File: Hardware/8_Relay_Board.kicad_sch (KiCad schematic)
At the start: 74 parts, among them J1 Conn_01x09, J10 Screw_Terminal_3.5mm_2, J2 Conn_01x09, J3 Screw_Terminal_3.5mm_4, J4 Screw_Terminal_3.5mm_4, J5 Screw_Terminal_3.5mm_4, J6 Screw_Terminal_3.5mm_4, J7 Screw_Terminal_3.5mm_4, J8 Screw_Terminal_3.5mm_4, J9 Barrel_Jack, U1 TLP627-4, U2 TLP627-4

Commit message: Close to finishing layout
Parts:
- removed J9: Barrel_Jack, SparkFun-Connector:POWER_JACK_PTH, symbol SparkFun-Connector:Barrel_Jack
- removed U1, U2: TLP627-4, SparkFun-Semiconductor-Standard:PDIP16, symbol SparkFun-IC-Special-Function:TLP627-4
- added J11: USB_C_Receptacle, SparkFun-Connector:USB-C-16P, symbol SparkFun-Connector:USB_C_Receptacle
- added R18, R19: 5.1k, SparkFun-Resistor:R_0603_1608Metric, symbol SparkFun-Resistor:5.1k_0603
- added U1, U2, U3, U4, U5, U6, U8, U9: TLP627, SparkFun-Semiconductor-Standard:DIP4, symbol SparkFun-IC-Special-Function:TLP627
- U7: footprint SparkFun-Aesthetic:Ordering_Instructions -> SparkFun-Aesthetic:ORDERING_INSTRUCTIONS
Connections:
- net +5V: now also J11.VBUS
- net COM1: now also J3.1 (Pin_1); no longer J3.2 (Pin_2)
- net COM2: now also J3.4 (Pin_4); no longer J4.1 (Pin_1)
- net COM3: now also J4.3 (Pin_3); no longer J4.4 (Pin_4)
- net COM4: now also J5.2 (Pin_2); no longer J5.3 (Pin_3)
- net COM5: now also J6.1 (Pin_1); no longer J6.2 (Pin_2)
- net COM6: now also J6.4 (Pin_4); no longer J7.1 (Pin_1)
- net COM7: now also J7.3 (Pin_3); no longer J7.4 (Pin_4)
- net COM8: now also J8.2 (Pin_2); no longer J8.3 (Pin_3)
- net GND: now also J11.GND, R18.2, R19.2, U1.3, U2.3, U3.3, U4.3, U5.3, U6.3, U8.3, U9.3
- net IN1: now also U3.1
- net IN2: now also U1.1
- net IN3: now also U2.1
- net IN4: now also U4.1
- net IN5: now also U5.1
- net IN6: now also U6.1
- net IN7: now also U8.1
- net IN8: now also U9.1
- net NC1: now also J3.2 (Pin_2); no longer J3.3 (Pin_3)
- net NC2: now also J4.1 (Pin_1); no longer J4.2 (Pin_2)
- net NC3: now also J4.4 (Pin_4); no longer J5.1 (Pin_1)
- net NC4: now also J5.3 (Pin_3); no longer J5.4 (Pin_4)
- net NC5: now also J6.2 (Pin_2); no longer J6.3 (Pin_3)
- net NC6: now also J7.1 (Pin_1); no longer J7.2 (Pin_2)
- net NC7: now also J7.4 (Pin_4); no longer J8.1 (Pin_1)
- net NC8: now also J8.3 (Pin_3); no longer J8.4 (Pin_4)
- net NO1: now also J3.3 (Pin_3); no longer J3.1 (Pin_1)
- net NO2: now also J4.2 (Pin_2); no longer J3.4 (Pin_4)
- net NO3: now also J5.1 (Pin_1); no longer J4.3 (Pin_3)
- net NO4: now also J5.4 (Pin_4); no longer J5.2 (Pin_2)
- net NO5: now also J6.3 (Pin_3); no longer J6.1 (Pin_1)
- net NO6: now also J7.2 (Pin_2); no longer J6.4 (Pin_4)
- net NO7: now also J8.1 (Pin_1); no longer J7.3 (Pin_3)
- net NO8: now also J8.4 (Pin_4); no longer J8.2 (Pin_2)
- net RELAY1: now also U4.4
- net RELAY2: now also U2.4
- net RELAY3: now also U1.4
- net RELAY4: now also U3.4
- net RELAY5: now also U9.4
- net RELAY6: now also U8.4
- net RELAY7: now also U6.4
- net RELAY8: now also U5.4
- net at R14.2: now also U6.2
- net at R10.2: now also U1.2
- net at R11.2: now also U2.2
- net at R13.2: now also U5.2
- net at R9.2: now also U3.2
- net at R16.2: now also U9.2
- net at R15.2: now also U8.2
- net at R12.2: now also U4.2
- new net: J11.A5 (CC1), R19.1
- new net: J11.B5 (CC2), R18.1
- new net: J11.A6 (D+), J11.B6 (D+)
- new net: J11.A7 (D-), J11.B7 (D-)
- new net: J11.A8 (NC), J11.B8 (NC)
- new net: J11.NC1 (NC), J11.NC2 (NC), J11.NC3 (NC)
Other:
- note added: "5VDC Input Header"
- note added: "USB Power Connector"
- note removed: "Power Connectors"
- moved on the sheet: D17, J10, JP9, R17

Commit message: Ready for final review
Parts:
- U1, U2, U3, U4, U5, U6, U8, U9: footprint SparkFun-Semiconductor-Standard:DIP4 -> SparkFun-Semiconductor-Standard:SMDIP4; symbol SparkFun-IC-Special-Function:TLP627 -> SparkFun-IC-Special-Function:TLP627(SMT)
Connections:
- net COM1: now also J3.2 (Pin_2); no longer J3.1 (Pin_1)
- net COM2: now also J4.1 (Pin_1); no longer J3.4 (Pin_4)
- net COM3: now also J4.4 (Pin_4); no longer J4.3 (Pin_3)
- net COM4: now also J5.3 (Pin_3); no longer J5.2 (Pin_2)
- net COM5: now also J6.2 (Pin_2); no longer J6.1 (Pin_1)
- net COM6: now also J7.1 (Pin_1); no longer J6.4 (Pin_4)
- net COM7: now also J7.4 (Pin_4); no longer J7.3 (Pin_3)
- net COM8: now also J8.3 (Pin_3); no longer J8.2 (Pin_2)
- net NC1: now also J3.1 (Pin_1); no longer J3.2 (Pin_2)
- net NC2: now also J3.4 (Pin_4); no longer J4.1 (Pin_1)
- net NC3: now also J4.3 (Pin_3); no longer J4.4 (Pin_4)
- net NC4: now also J5.2 (Pin_2); no longer J5.3 (Pin_3)
- net NC5: now also J6.1 (Pin_1); no longer J6.2 (Pin_2)
- net NC6: now also J6.4 (Pin_4); no longer J7.1 (Pin_1)
- net NC7: now also J7.3 (Pin_3); no longer J7.4 (Pin_4)
- net NC8: now also J8.2 (Pin_2); no longer J8.3 (Pin_3)

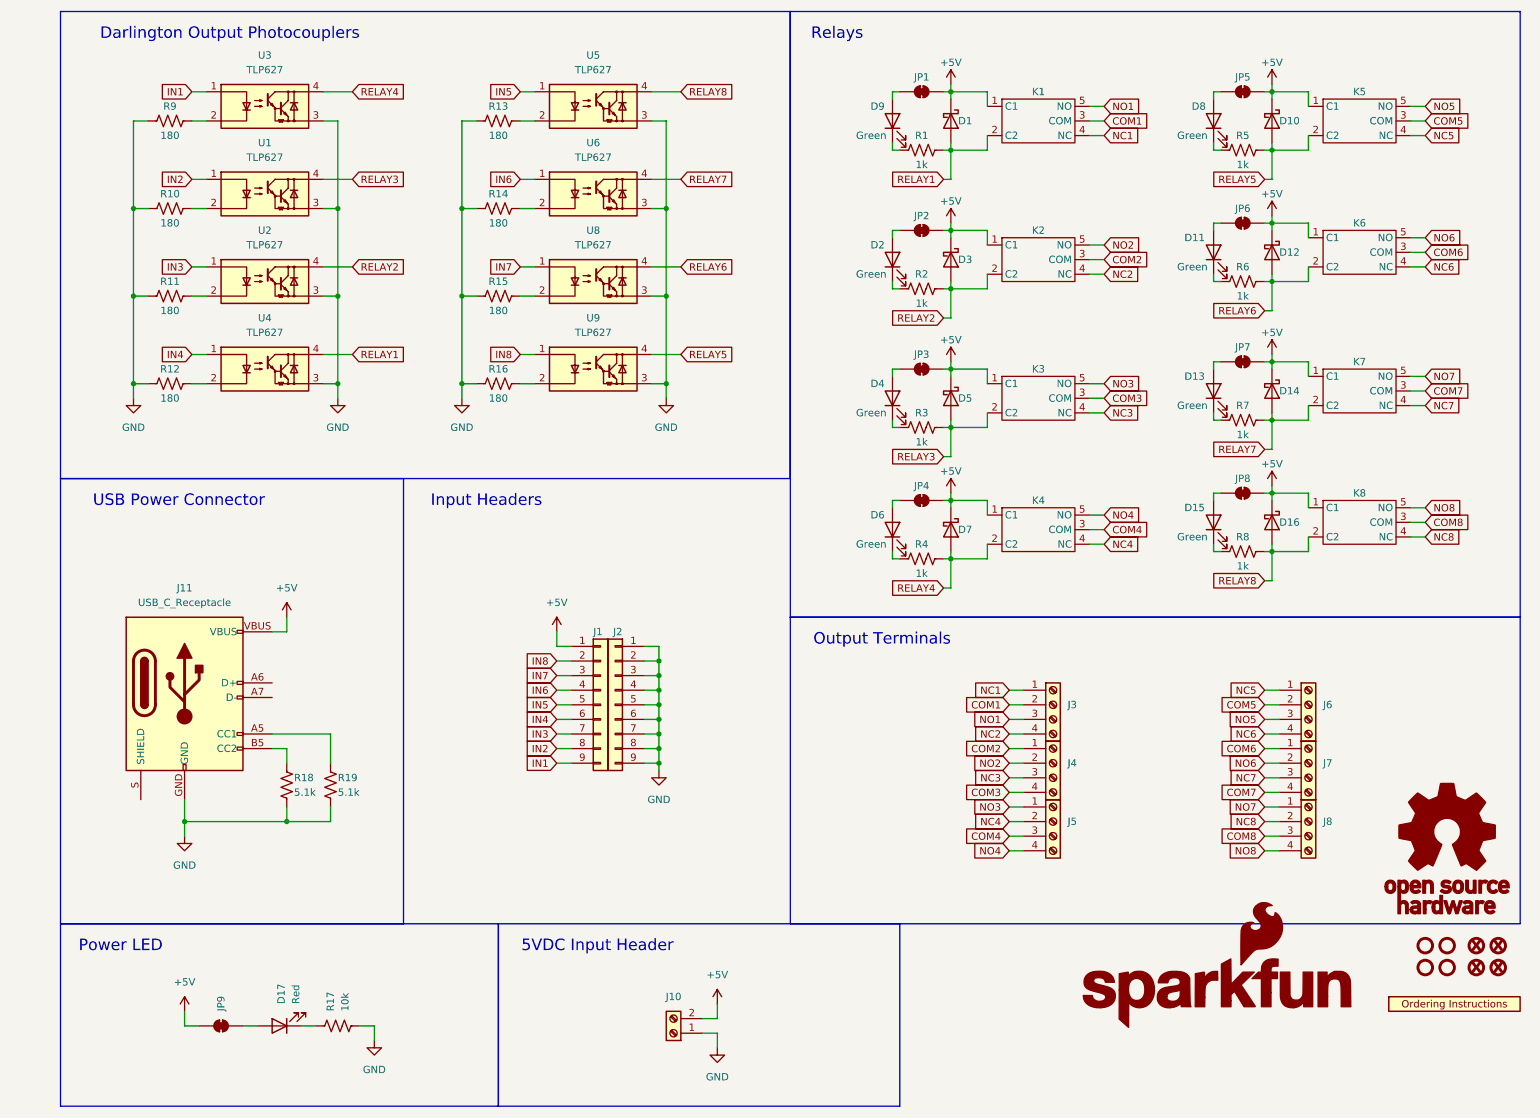
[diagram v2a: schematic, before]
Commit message: Second pre-release revision
- Add isolation under relays
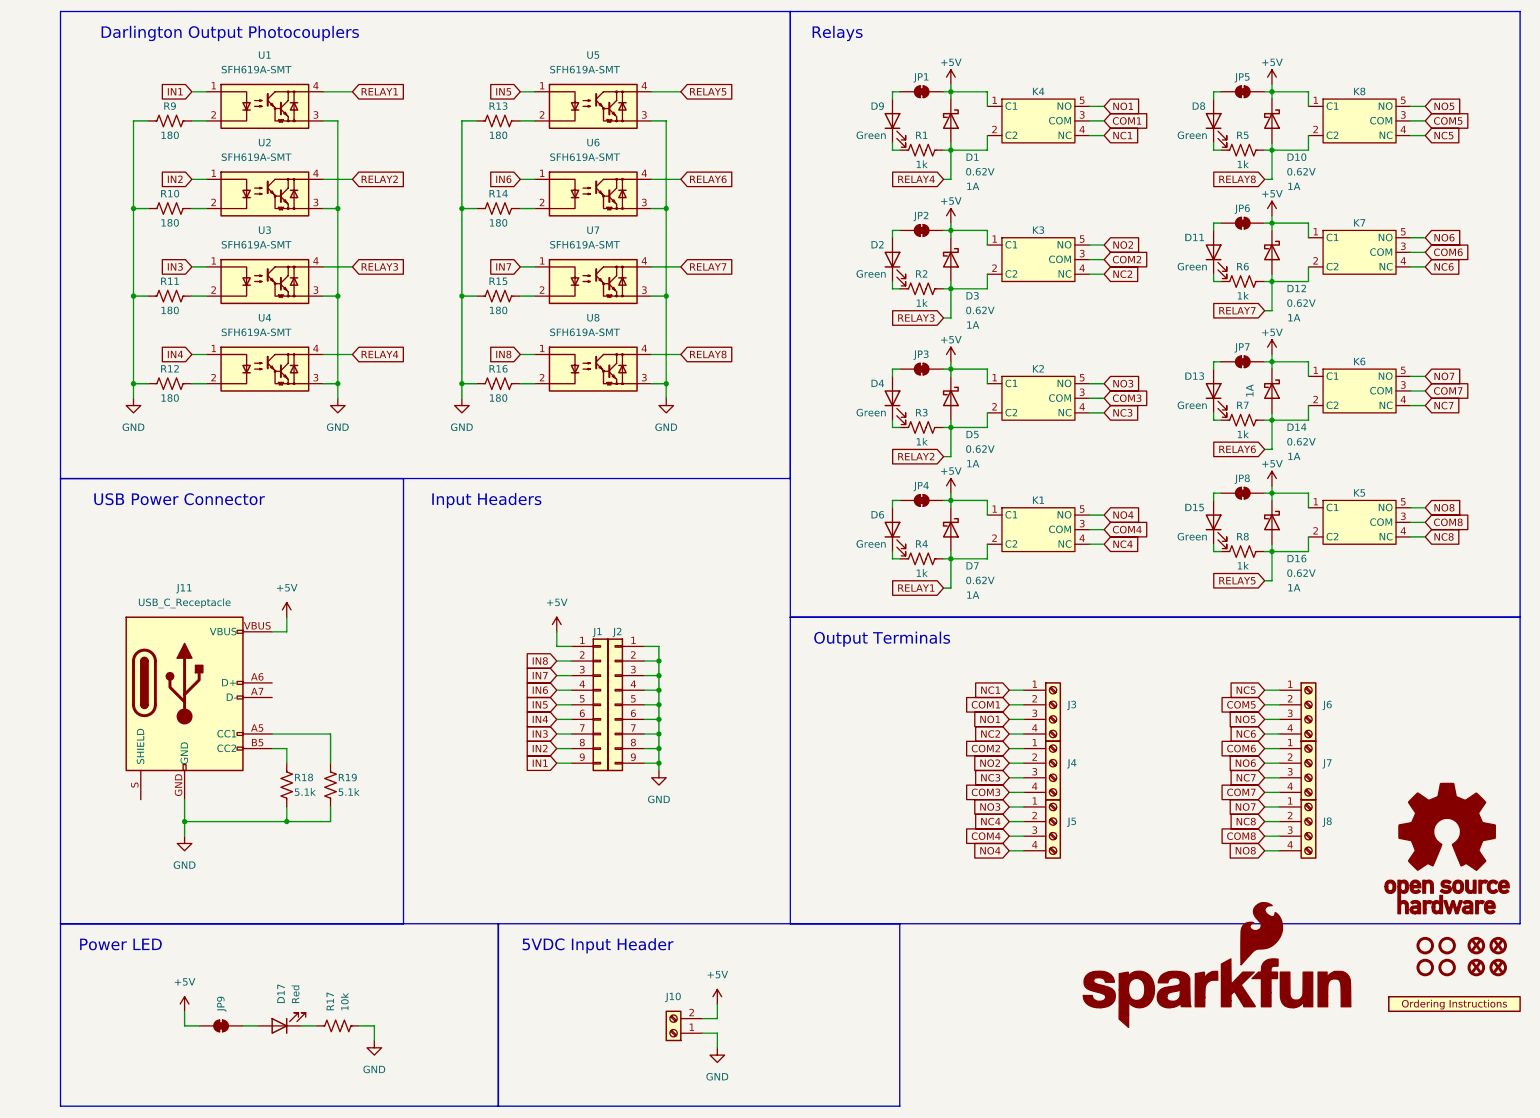
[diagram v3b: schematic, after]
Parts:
- D1, D10, D12, D16, D3, D5, D7: Current (none) -> 1A; VForward (none) -> 0.62V; VReverse (none) -> 23V
- D14: Current (none) -> 1A; Forward Current (none) -> 1A; Reverse Voltage (none) -> 23V; VForward (none) -> 0.62V; VReverse (none) -> 23V
- JP1, JP2, JP3, JP4, JP5, JP6, JP7, JP8, JP9: footprint SparkFun-Jumper:SMT-JUMPER_2_NC_TRACE_NO-SILK -> SparkFun-Jumper:SMT-JUMPER_2_NC_TRACE_SILK; symbol SparkFun-Jumper:SolderJumper_2_Bridged_No_Silk -> SparkFun-Jumper:SolderJumper_2_Bridged
- U1: renamed from U3; value TLP627 -> SFH619A-SMT; footprint SparkFun-Semiconductor-Standard:SMDIP4 -> SparkFun-Semiconductor-Standard:SMDIP4-WIDE; symbol SparkFun-IC-Special-Function:TLP627(SMT) -> SparkFun-IC-Special-Function:SFH619A-SMT
- U2: renamed from U1; value TLP627 -> SFH619A-SMT; footprint SparkFun-Semiconductor-Standard:SMDIP4 -> SparkFun-Semiconductor-Standard:SMDIP4-WIDE; symbol SparkFun-IC-Special-Function:TLP627(SMT) -> SparkFun-IC-Special-Function:SFH619A-SMT
- U3: renamed from U2; value TLP627 -> SFH619A-SMT; footprint SparkFun-Semiconductor-Standard:SMDIP4 -> SparkFun-Semiconductor-Standard:SMDIP4-WIDE; symbol SparkFun-IC-Special-Function:TLP627(SMT) -> SparkFun-IC-Special-Function:SFH619A-SMT
- U4, U5, U6: value TLP627 -> SFH619A-SMT; footprint SparkFun-Semiconductor-Standard:SMDIP4 -> SparkFun-Semiconductor-Standard:SMDIP4-WIDE; symbol SparkFun-IC-Special-Function:TLP627(SMT) -> SparkFun-IC-Special-Function:SFH619A-SMT
- U7: renamed from U8; value TLP627 -> SFH619A-SMT; footprint SparkFun-Semiconductor-Standard:SMDIP4 -> SparkFun-Semiconductor-Standard:SMDIP4-WIDE; symbol SparkFun-IC-Special-Function:TLP627(SMT) -> SparkFun-IC-Special-Function:SFH619A-SMT
- U8: renamed from U9; value TLP627 -> SFH619A-SMT; footprint SparkFun-Semiconductor-Standard:SMDIP4 -> SparkFun-Semiconductor-Standard:SMDIP4-WIDE; symbol SparkFun-IC-Special-Function:TLP627(SMT) -> SparkFun-IC-Special-Function:SFH619A-SMT
- renumbered K4 to K1, K3 to K2, K2 to K3, K1 to K4, K8 to K5, K7 to K6, K6 to K7, K5 to K8, U7 to U9
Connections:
- net RELAY1: now also D7.A, K1.2 (C2), R4.2, U1.4; no longer D1.A, K4.2 (C2), R1.2, U4.4
- net RELAY2: now also D5.A, K2.2 (C2), R3.2, U2.4; no longer D3.A, K3.2 (C2), R2.2, U3.4
- net RELAY3: now also D3.A, K3.2 (C2), R2.2, U3.4; no longer D5.A, K2.2 (C2), R3.2, U2.4
- net RELAY4: now also D1.A, K4.2 (C2), R1.2, U4.4; no longer D7.A, K1.2 (C2), R4.2, U1.4
- net RELAY5: now also D16.A, K5.2 (C2), R8.2, U5.4; no longer D10.A, K8.2 (C2), R5.2, U8.4
- net RELAY6: now also D14.A, K6.2 (C2), R7.2, U6.4; no longer D12.A, K7.2 (C2), R6.2, U7.4
- net RELAY7: now also D12.A, K7.2 (C2), R6.2, U7.4; no longer D14.A, K6.2 (C2), R7.2, U6.4
- net RELAY8: now also D10.A, K8.2 (C2), R5.2, U8.4; no longer D16.A, K5.2 (C2), R8.2, U5.4
